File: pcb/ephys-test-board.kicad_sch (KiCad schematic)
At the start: 9 parts, among them J1 10129383-910002ALF, J8 BM03B-SRSS-TB

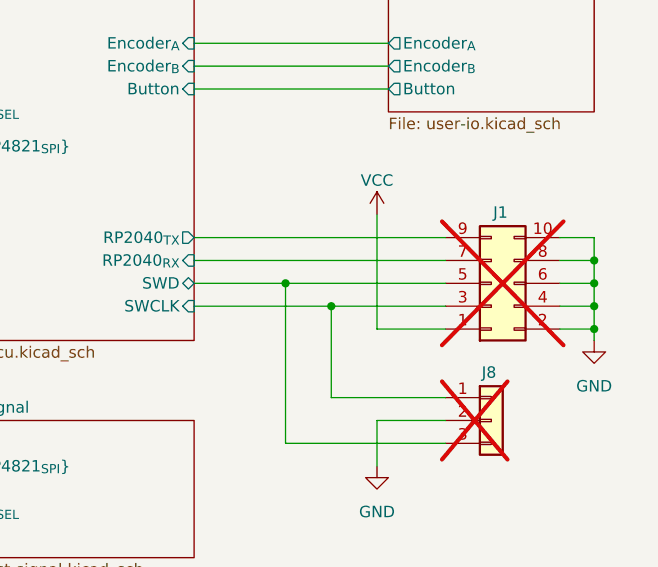
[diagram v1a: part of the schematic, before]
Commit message: Address issues with case found during proptyping
- Add recess for reset button
- Add 3.5V power managment circuit and simplify on/off switch debounce
- Increase space in bottom porition of case for thicker battery
- Remove alignment notches from PCB -- uses features of case instead
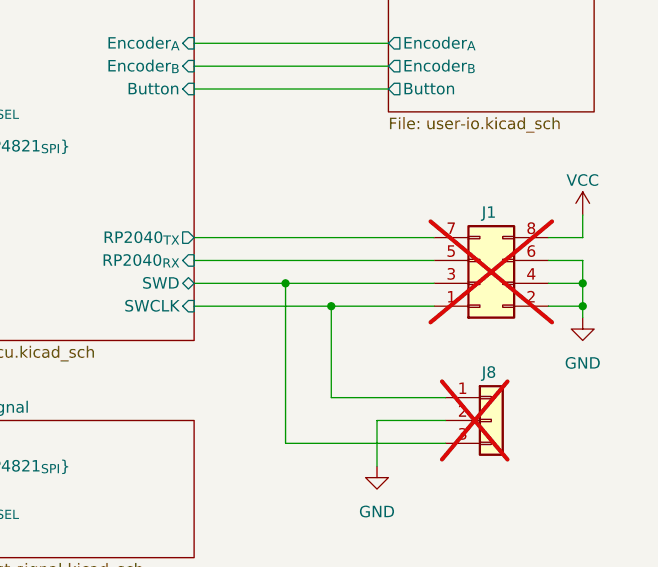
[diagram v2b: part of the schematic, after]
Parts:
- J1: footprint Connector_PinHeader_2.54mm:PinHeader_2x05_P2.54mm_Vertical_SMD -> Connector_PinHeader_2.54mm:PinHeader_2x04_P2.54mm_Vertical_SMD; symbol Connector_Generic:Conn_02x05_Odd_Even -> Connector_Generic:Conn_02x04_Odd_Even
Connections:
- net GND: no longer J1.10 (Pin_10), J1.8 (Pin_8)
- net MCU/RP2040_{RX}: now also J1.5 (Pin_5); no longer J1.7 (Pin_7)
- net MCU/RP2040_{TX}: now also J1.7 (Pin_7); no longer J1.9 (Pin_9)
- net MCU/SWCLK: now also J1.1 (Pin_1); no longer J1.3 (Pin_3)
- net MCU/SWD: now also J1.3 (Pin_3); no longer J1.5 (Pin_5)
- net VCC: now also J1.8 (Pin_8); no longer J1.1 (Pin_1)

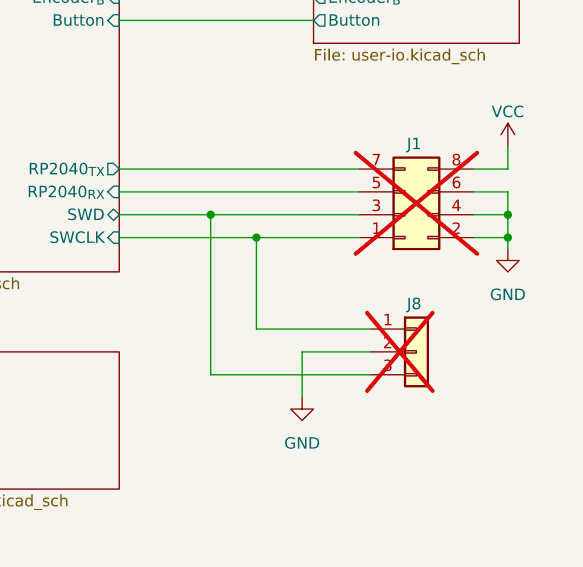
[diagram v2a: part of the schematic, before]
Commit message: Added OEPS PN.
Co-Authored-By: David Palma <78764277+davidpalma666@users.noreply.github.com>
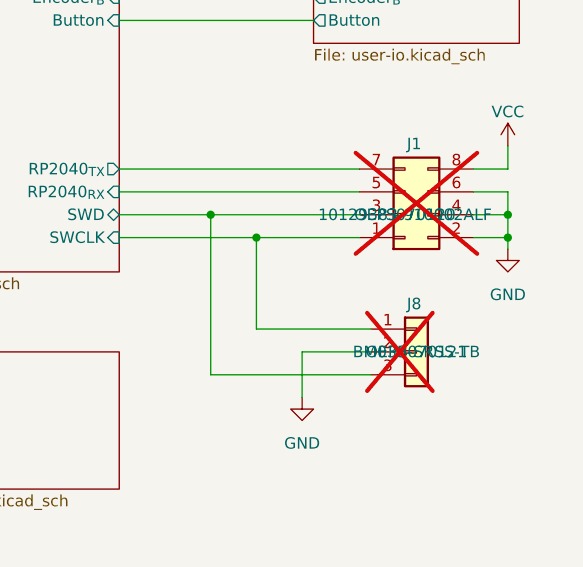
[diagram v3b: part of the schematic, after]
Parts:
- J1: value 10129383-910002ALF -> DNP; MPN (none) -> 10129383-910002ALF; OEPSPN (none) -> OEPS070120
- J8: value BM03B-SRSS-TB -> DNP; MPN (none) -> BM03B-SRSS-TB; OEPSPN (none) -> OEPS070121
- TP11, TP12: now left out of the parts list

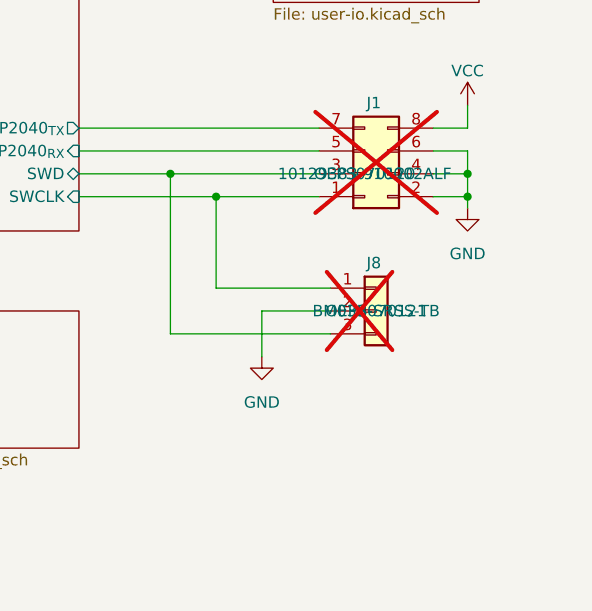
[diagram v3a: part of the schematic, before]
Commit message: Minor edits during BOM review
- Remove DNP in value fields since a dedicated channel is provided for
  that information
- Add MP pins to header symbols
- Update BOM and PDFs
- New gerbers to connect mount points to headers. No component position
  changes
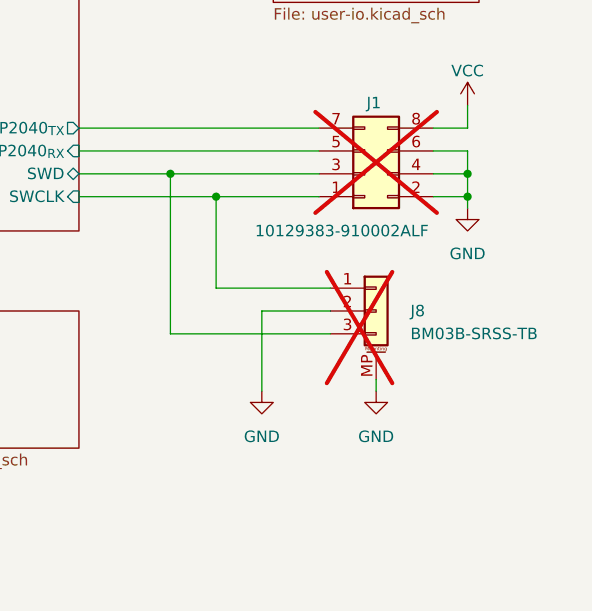
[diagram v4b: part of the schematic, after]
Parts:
- J1: value DNP -> 10129383-910002ALF
- J8: value DNP -> BM03B-SRSS-TB; symbol Connector_Generic:Conn_01x03 -> Connector_Generic_MountingPin:Conn_01x03_MountingPin
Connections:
- net GND: now also J8.MP (MountPin)

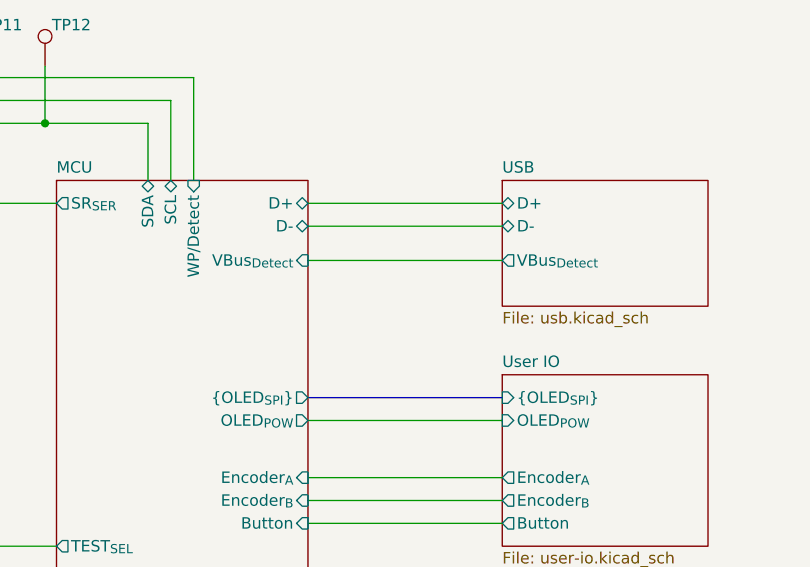
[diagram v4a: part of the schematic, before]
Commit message: Add battery measurement circuit
- Measure battery voltage using microcontroller's ADC
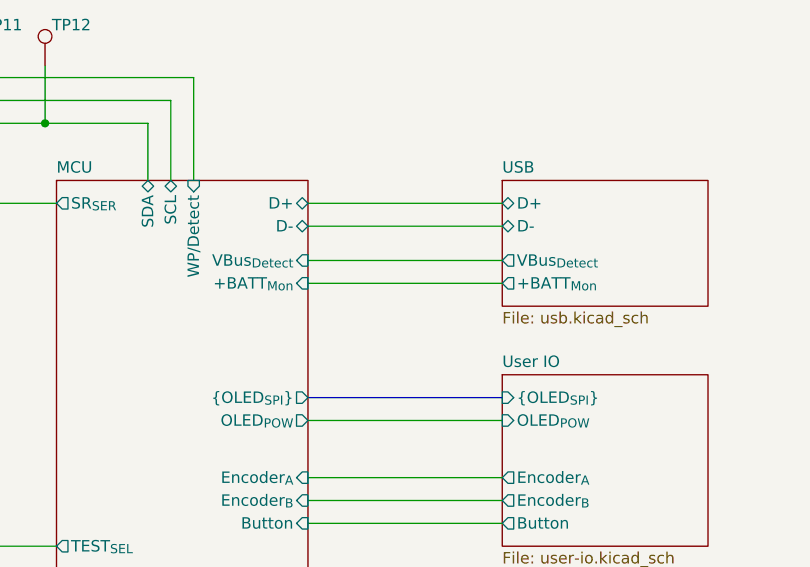
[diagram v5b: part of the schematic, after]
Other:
- sheet MCU ports: added +BATT_{Mon}; removed none
- sheet USB ports: added +BATT_{Mon}; removed none
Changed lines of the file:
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@@
 	(title_block
 		(title "Extracellular Electrophysiology Test Board")
-		(rev "C")
+		(rev "D")
 		(company "Open Ephys, Inc")
 		(comment 1 "Jonathan P. Newman")
@@
 	(wire
 		(pts
+			(xy 219.71 49.53) (xy 241.3 49.53)
+		)
+		(stroke
+			(width 0)
+			(type default)
+		)
+	)
+	(wire
+		(pts
 			(xy 229.87 115.57) (xy 229.87 97.79)
 		)
@@
 			)
 		)
+		(pin "+BATT_{Mon}" output
+			(at 241.3 49.53 180)
+			(effects
+				(font
+					(size 1.27 1.27)
+				)
+				(justify left)
+			)
+		)
 		(instances
 			(project "ephys-test-board"
@@
 			(effects
 				(font
+					(size 1.27 1.27)
+				)
+				(justify right)
+			)
+		)
+		(pin "+BATT_{Mon}" input
+			(at 219.71 49.53 0)
+			(effects
+				(font

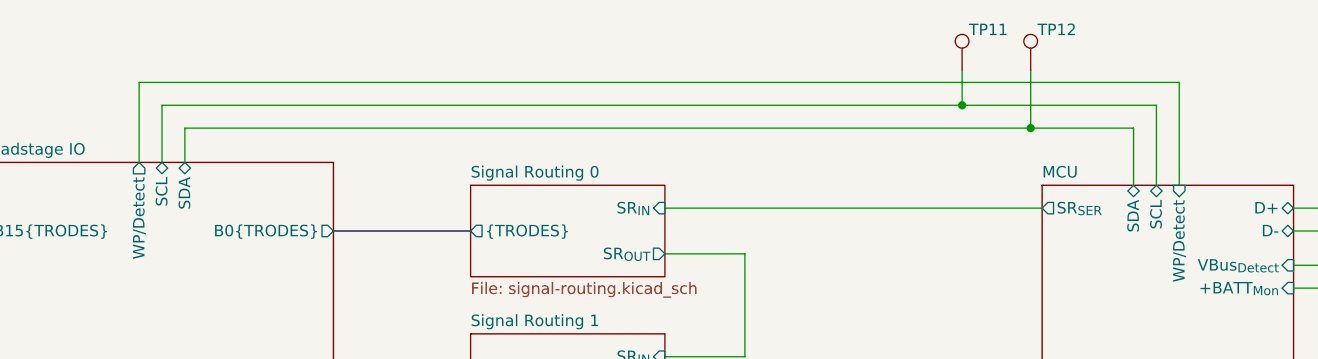
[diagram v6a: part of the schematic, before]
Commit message: Use 1.25V reference voltage for electrode test signal
- This prevents large AC component when channel switch occurs.
- Previously the attenuator reference and nomimal electrode signals were
  both ground. Since the test signal is centered arround 1.25V, there
  the test signal is effectively a 1.25V square wave + the indented
  signal. The square waves edges were readily passed through the AC
  coupling capacitor.
- Add LCSC numbers to all required components for assembly.
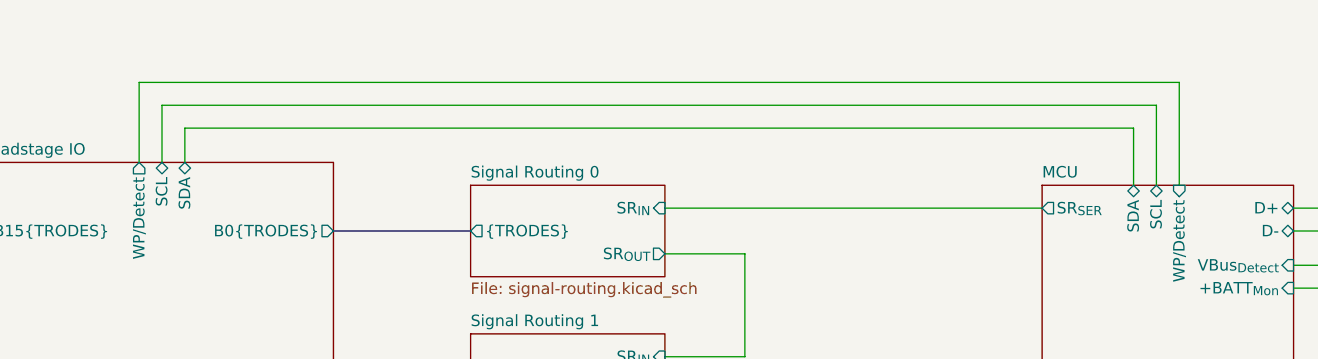
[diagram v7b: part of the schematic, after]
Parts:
- removed TP11, TP12: VCC, TestPoint:TestPoint_Pad_D2.0mm, symbol Connector:TestPoint
- J1, J8: now left out of the parts list

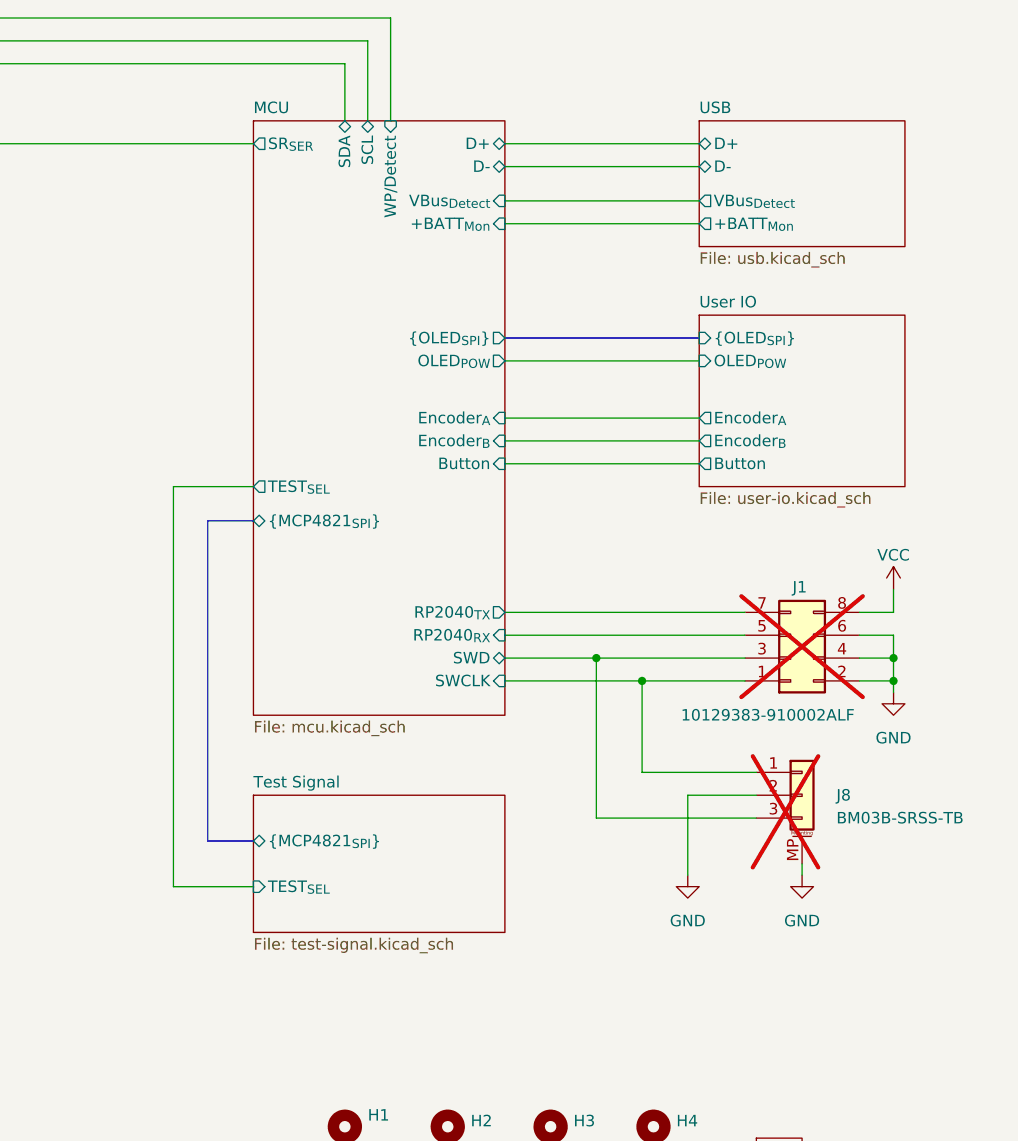
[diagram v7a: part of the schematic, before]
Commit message: Implmenent bipolar test signal
- Generate internal negative rail
- Shift DAC output by VREF/2
- Replace analog switches with depletion mode switches to allow negative
  signals
- DC couple electrode inputs
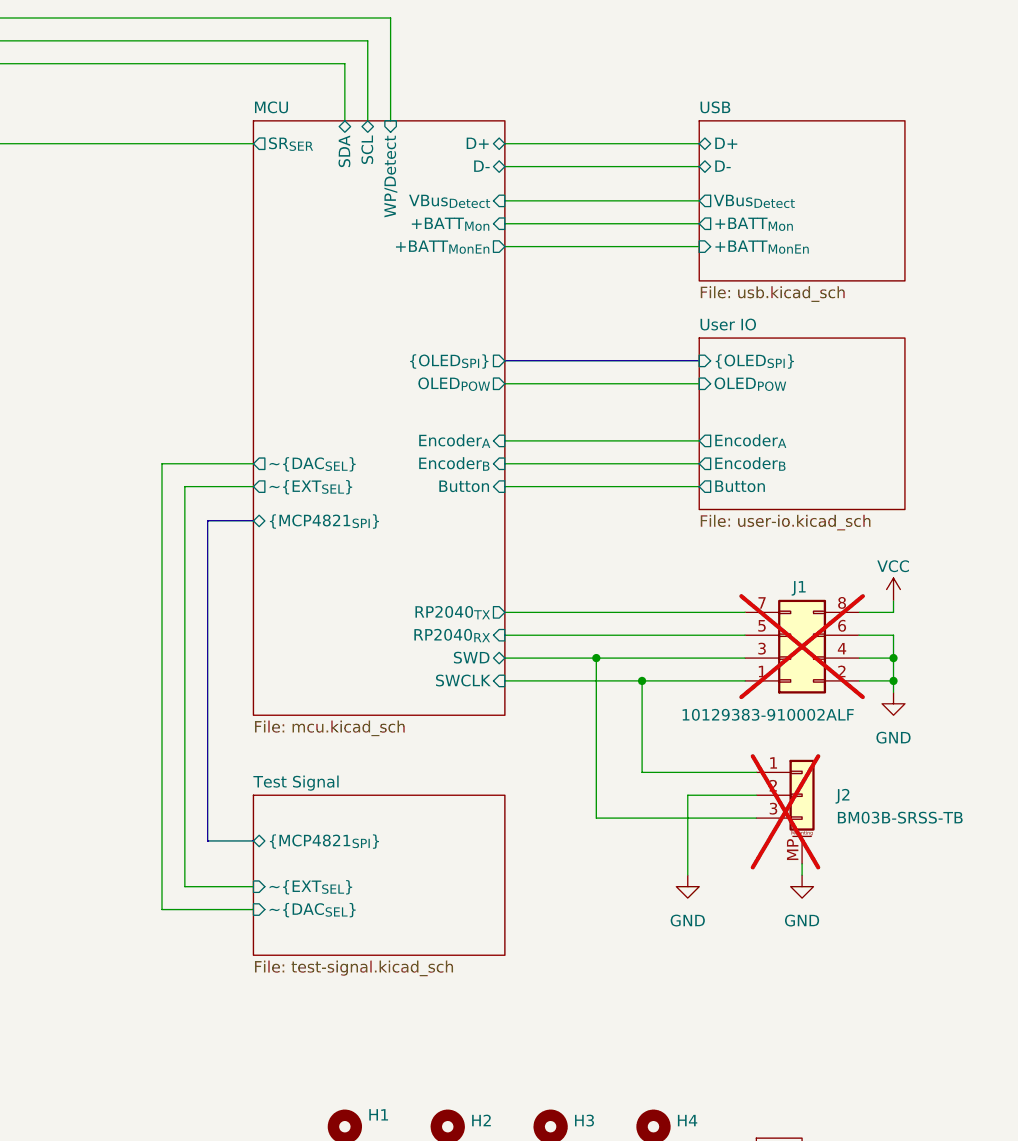
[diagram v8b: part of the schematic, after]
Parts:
- renumbered J8 to J2
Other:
- sheet MCU ports: added +BATT_{MonEn}, ~{DAC_{SEL}}, ~{EXT_{SEL}}; removed TEST_{SEL}
- sheet Test Signal ports: added ~{DAC_{SEL}}, ~{EXT_{SEL}}; removed TEST_{SEL}
- sheet USB ports: added +BATT_{MonEn}; removed none
